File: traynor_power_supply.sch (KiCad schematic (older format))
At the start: 33 parts, among them J1 AC IN, J10 OUT2, J11 OUT3, J2 AC IN, J3 Chassis GND, J4 OUT1, J5 TREM, J6 SW, J7 SW, J8 CHOKE, J9 CHOKE

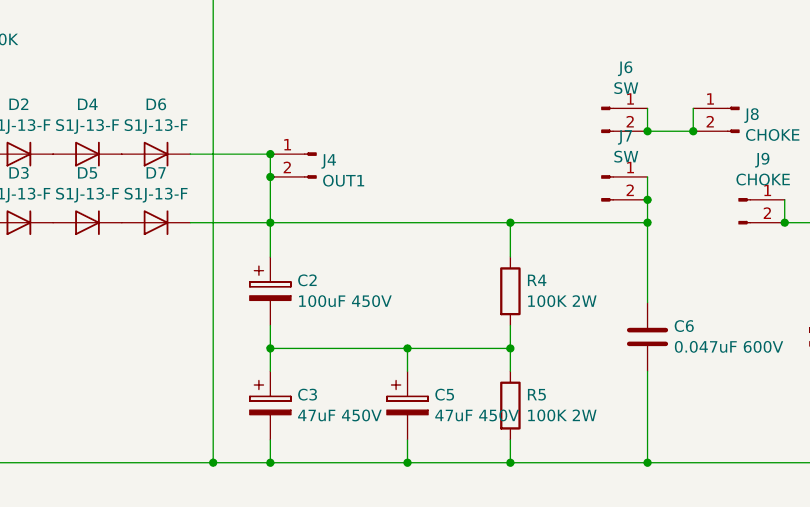
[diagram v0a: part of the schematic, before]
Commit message: change the 100uF capacitor to be 2 47uF capacitors
find there was a capacitor without a footprint on the schematic too, so we were missing it before.
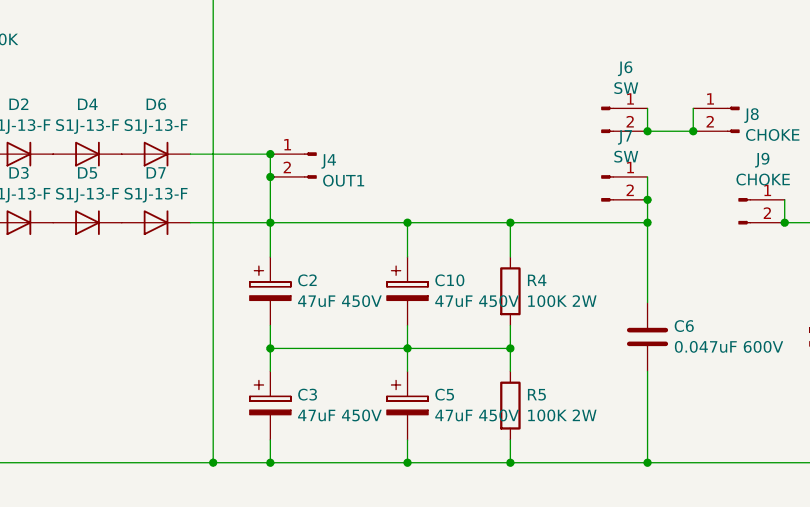
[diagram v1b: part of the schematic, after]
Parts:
- added C10: 47uF 450V, Capacitor_THT:CP_Radial_D12.5mm_P5.00mm, symbol Device:CP
- C2: value 100uF 450V -> 47uF 450V; footprint Capacitor_THT:CP_Radial_D18.0mm_P7.50mm -> Capacitor_THT:CP_Radial_D12.5mm_P5.00mm
- C3: footprint (none) -> Capacitor_THT:CP_Radial_D12.5mm_P5.00mm
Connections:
- net at C2.1, C6.1, D6.1 (K)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: now also C10.1
- net at C2.2, C3.1, C5.1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: now also C10.2
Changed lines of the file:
@@
 F 0 "C3" H 3468 4646 50  0000 L CNN
 F 1 "47uF 450V" H 3468 4555 50  0000 L CNN
-F 2 "" H 3388 4450 50  0001 C CNN
+F 2 "Capacitor_THT:CP_Radial_D12.5mm_P5.00mm" H 3388 4450 50  0001 C CNN
 F 3 "~" H 3350 4600 50  0001 C CNN
 	1    3350 4600
@@
 P 3350 4100
 F 0 "C2" H 3468 4146 50  0000 L CNN
-F 1 "100uF 450V" H 3468 4055 50  0000 L CNN
-F 2 "Capacitor_THT:CP_Radial_D18.0mm_P7.50mm" H 3388 3950 50  0001 C CNN
+F 1 "47uF 450V" H 3468 4055 50  0000 L CNN
+F 2 "Capacitor_THT:CP_Radial_D12.5mm_P5.00mm" H 3388 3950 50  0001 C CNN
 F 3 "~" H 3350 4100 50  0001 C CNN
 	1    3350 4100
@@
 Connection ~ 3350 3800
 Wire Wire Line
-	3350 3800 4400 3800
+	3350 3800 3950 3800
 Wire Wire Line
 	4400 3800 4400 3950
@@
 Connection ~ 1600 3500
 Connection ~ 1600 3800
+$Comp
+L Device:CP C10
+U 1 1 5C539BD9
+P 3950 4100
+F 0 "C10" H 4068 4146 50  0000 L CNN
+F 1 "47uF 450V" H 4068 4055 50  0000 L CNN
+F 2 "Capacitor_THT:CP_Radial_D12.5mm_P5.00mm" H 3988 3950 50  0001 C CNN
+F 3 "~" H 3950 4100 50  0001 C CNN
+	1    3950 4100
+	1    0    0    -1
+$EndComp
+Wire Wire Line
+	3950 4250 3950 4350
+Wire Wire Line
+	3950 3950 3950 3800
+Connection ~ 3950 3800
+Wire Wire Line
+	3950 3800 4400 3800
 $EndSCHEMATC
